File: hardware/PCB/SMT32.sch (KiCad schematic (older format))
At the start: 26 parts, among them J1 473460001, SW1 B3U-1000P, SW2 B3U-1000P, U3 AZ1117CH-3.3TRG1, U4 STM32F303CCT6, Y1 8Mhz20pF

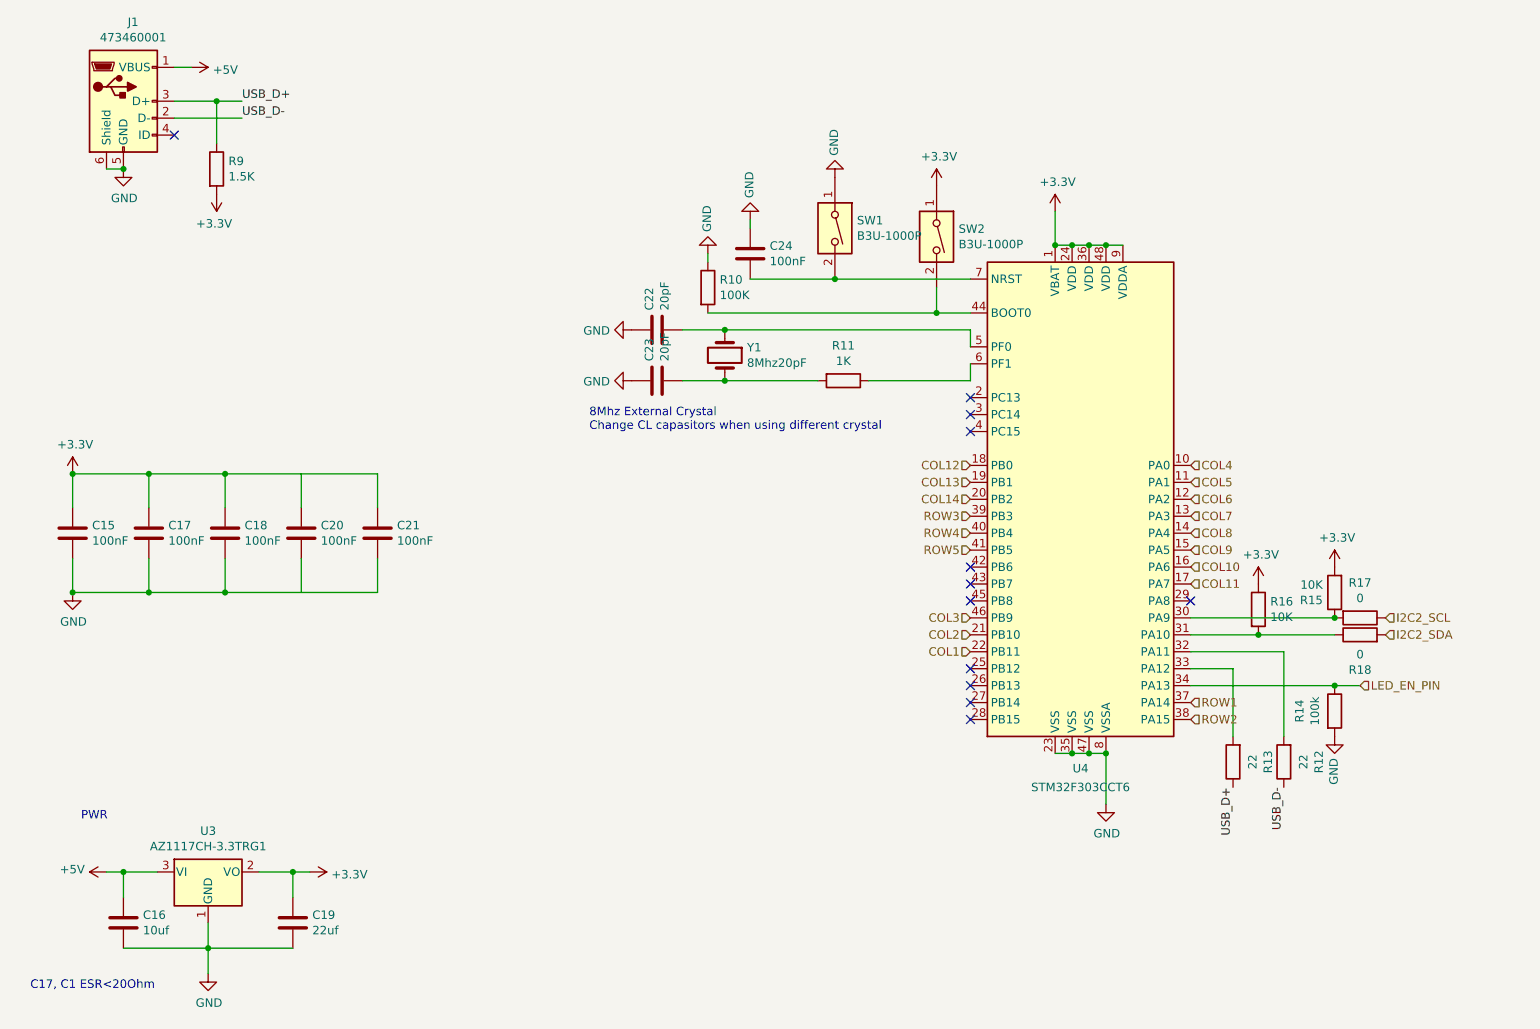
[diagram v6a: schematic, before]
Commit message: update render, remove useless files, fix the decoupeling
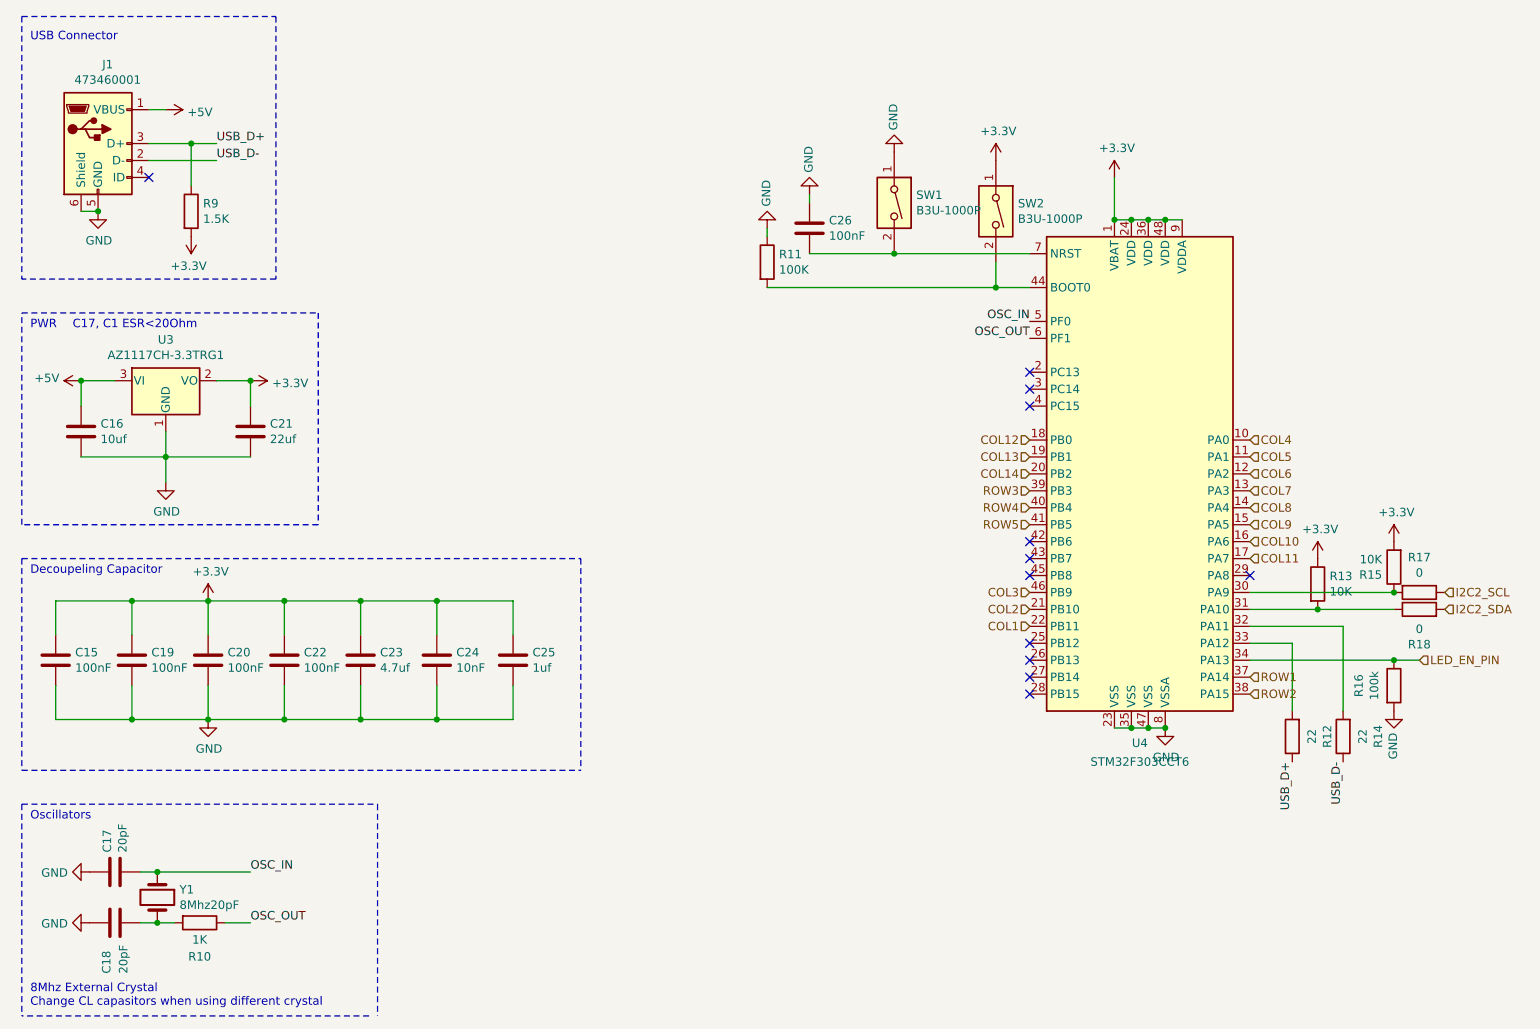
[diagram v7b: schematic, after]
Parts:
- added C24: 10nF, Capacitor_SMD:C_0402_1005Metric, symbol Device:C
- added C25: 1uf, Capacitor_SMD:C_0402_1005Metric, symbol Device:C
- C23: renamed from C21; value 100nF -> 4.7uf
- renumbered C22 to C17, C23 to C18, C17 to C19, C18 to C20, C19 to C21, C20 to C22, C24 to C26, R11 to R10, R10 to R11, R13 to R12, R16 to R13, R12 to R14, R14 to R16
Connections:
- net +3V3: now also C24.1, C25.1
- net GND: now also C24.2, C25.2
- net OSC_IN: now reaches C17.2, U4.5 (PF0), Y1.1
- net OSC_OUT: now reaches R10.1, U4.6 (PF1)
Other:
- note added: "Decoupeling Capacitor"
- note added: "Oscillators"
- note added: "USB Connector"
- moved on the sheet: C15, C16, C17, C18, C19, C20, C21, C22, C23, C26, J1, R10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

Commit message: small improvements (cap distance)
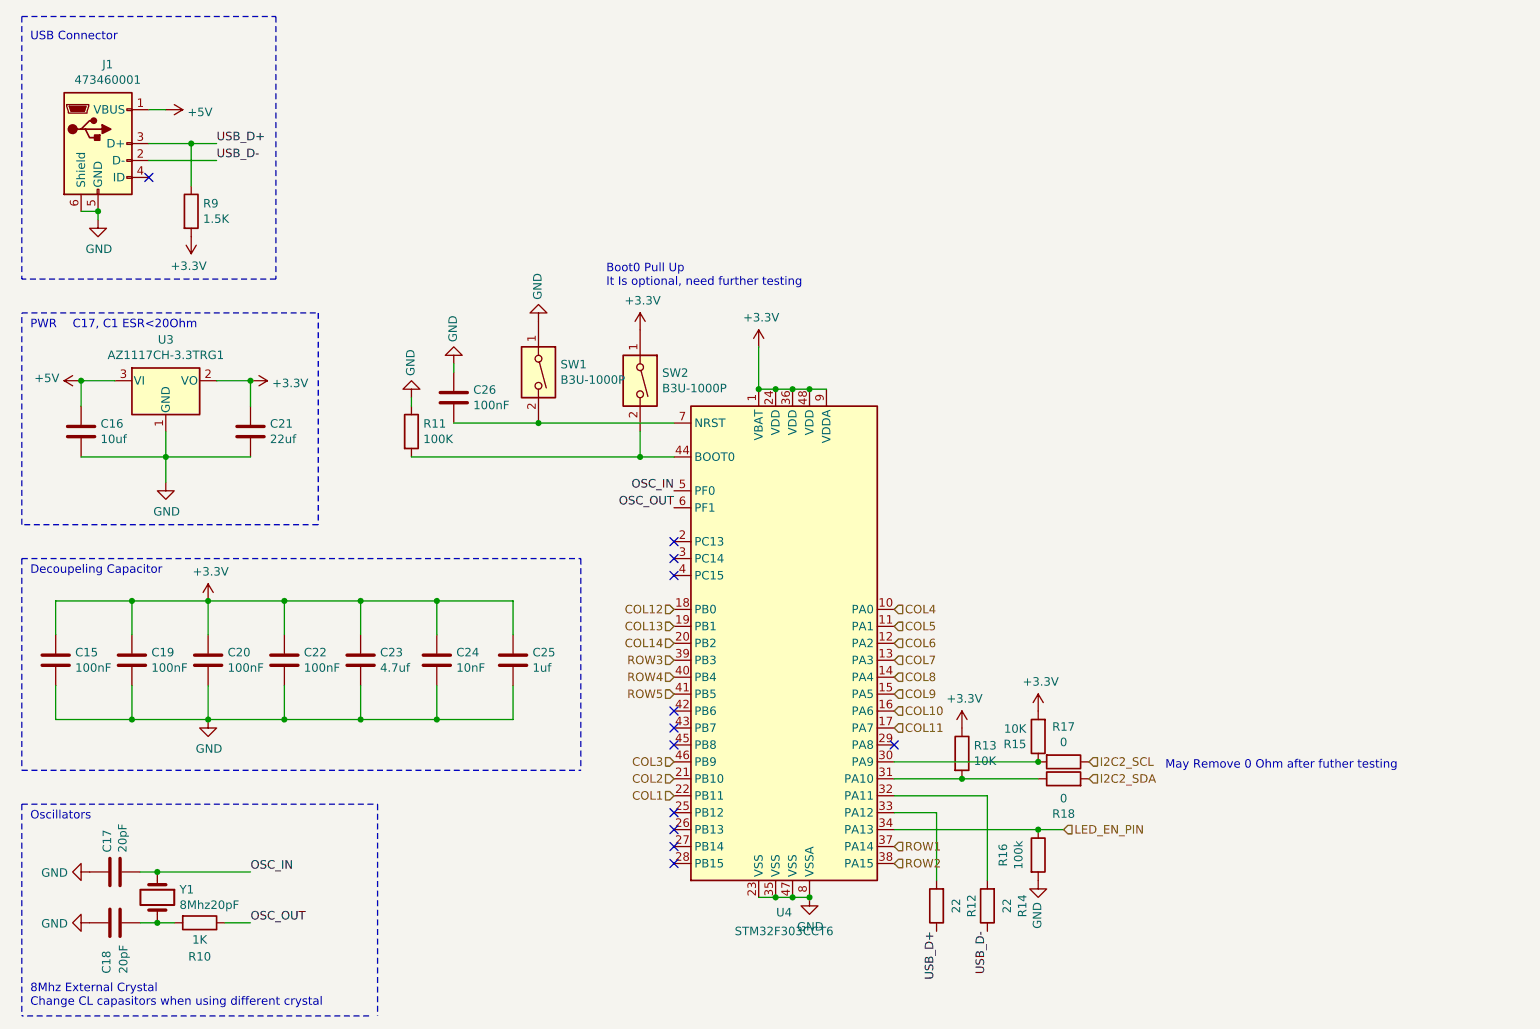
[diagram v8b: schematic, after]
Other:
- note added: "Boot0 Pull Up \nIt Is optional, need further testing"
- note added: "May Remove 0 Ohm after futher testing"
- moved on the sheet: C26, R11, R12, R13, R14, R15, R16, R17, R18, SW1, SW2, U4
